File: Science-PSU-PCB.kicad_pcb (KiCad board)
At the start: 2 copper layers, 100 x 90.8 mm, 43 parts, among them J1 XT60-M, J2 ESTOP, J3 ON, J4 XT60-M, J5 XT60-M, J6 XT60-M, J7 Conn_01x04, J8 Screw_Terminal_01x02, J9 Screw_Terminal_01x02, Q1 MMBT3904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

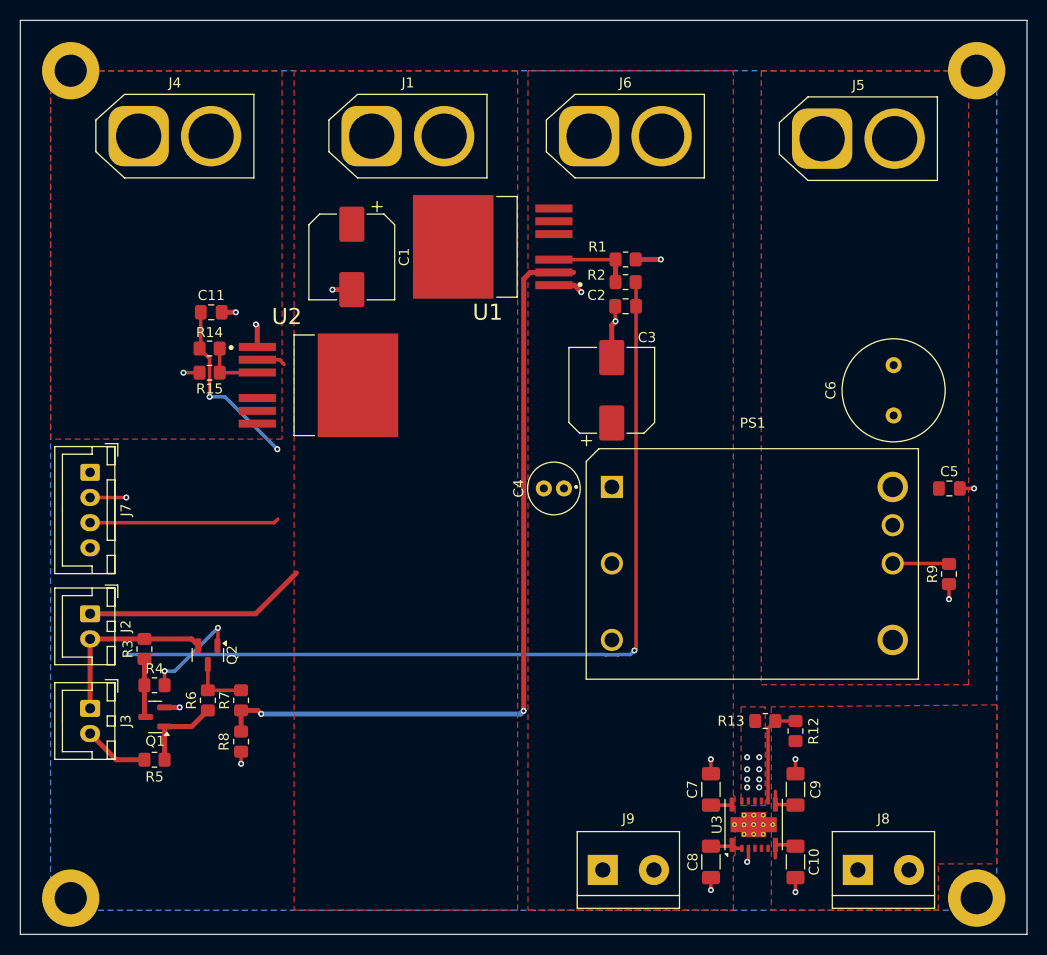
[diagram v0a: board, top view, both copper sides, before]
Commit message: Changed vertical to horizontal connectors
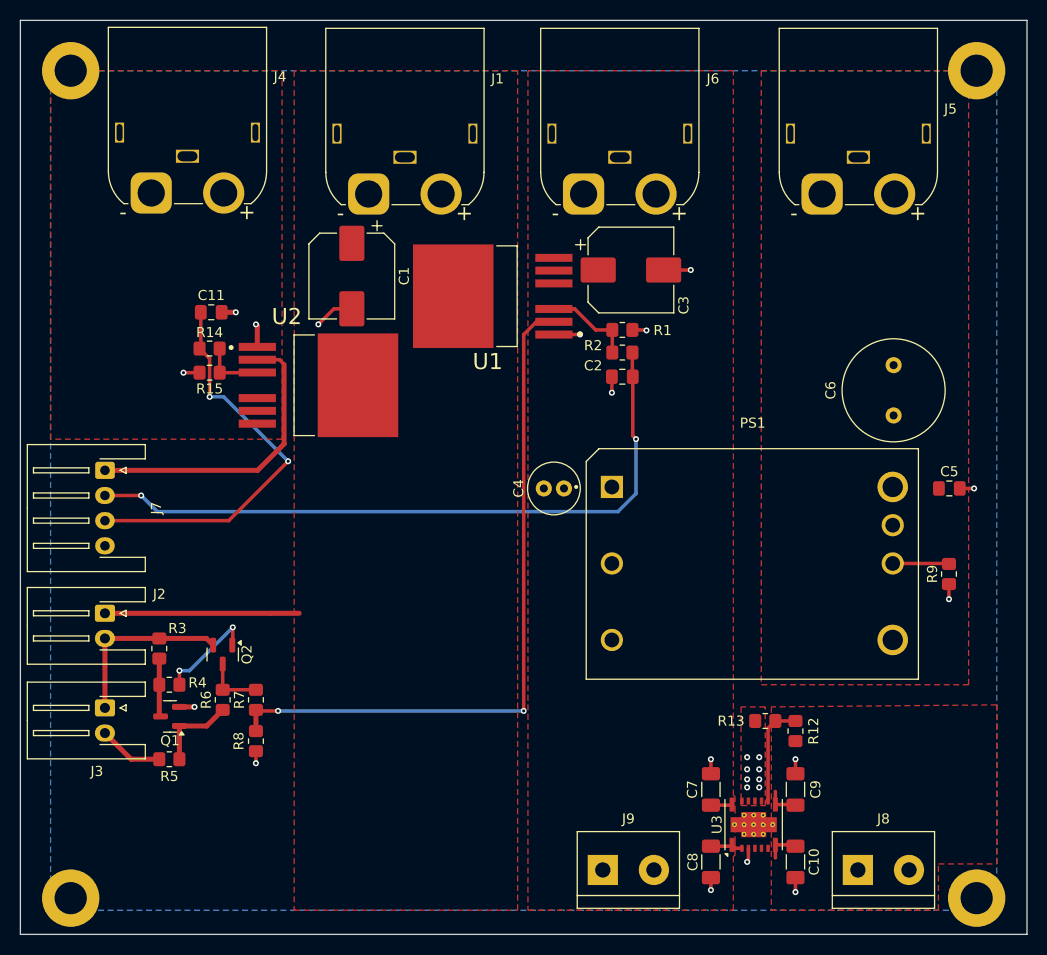
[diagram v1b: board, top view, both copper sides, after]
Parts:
- J1, J4, J5, J6: footprint Connector_AMASS:AMASS_XT60-M_1x02_P7.20mm_Vertical -> Connector_AMASS:AMASS_XT60IPW-M_1x03_P7.20mm_Horizontal
- J2, J3: footprint Connector_JST:JST_XH_B2B-XH-A_1x02_P2.50mm_Vertical -> Connector_JST:JST_XH_S2B-XH-A-1_1x02_P2.50mm_Horizontal
- J7: footprint Connector_JST:JST_XH_B4B-XH-A_1x04_P2.50mm_Vertical -> Connector_JST:JST_XH_S4B-XH-A-1_1x04_P2.50mm_Horizontal
- moved C3 12.1 mm to (100.7, 69.8), turned to 0 degrees
- moved C2 7.01 mm to (99.8, 80.4)
- moved R1 7.01 mm to (99.8, 75.8)
- moved R2 7.01 mm to (99.8, 78.0)
- moved J4 5.79 mm to (53.0, 62.1)
- moved J6 5.78 mm to (96.0, 62.2)
- moved J1 5.76 mm to (74.6, 62.2)
- moved J5 5.50 mm to (119.7, 62.2)
- moved U1 4.90 mm to (86.9, 72.4)
- moved C1 1.90 mm to (72.9, 70.4)
- moved J7 1.49 mm to (48.4, 89.7)
- moved R8 1.48 mm to (63.4, 116.6)
- moved J2 1.48 mm to (48.4, 103.9)
- moved J3 1.48 mm to (48.4, 113.3)
- moved Q2 1.48 mm to (60.1, 108.0)
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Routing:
- net /HE_CTRL: track 2.85 -> 29.6 mm
- net /PWR_CTRL_IS: track 90.9 -> 68.3 mm
- net /PWR_CTRL: track 78.6 -> 69.7 mm
- net /HE_IS: track 36.7 -> 40.0 mm
- net 24V_BAT: track 22.2 -> 19.3 mm
- net Net-(U1-IS): track 8.38 -> 8.94 mm
- net GND: track 30.6 -> 30.2 mm, vias 24 -> 25
